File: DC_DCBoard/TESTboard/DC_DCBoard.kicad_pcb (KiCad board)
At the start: 2 copper layers, 137.2 x 68.6 mm, 26 parts, among them J1 TSV, J2 12V_OUT, J3 Conn_01x05, U1 DCM4623TD2J13D0T70, U2 LTV-817S, U3 TLP184, U4 LTV-817S

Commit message: Fixed pot value on test board
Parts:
- added R2: 6.8k, Resistor_SMD:R_0603_1608Metric, F.Cu at (106.0, 127.6)
- RV1: value 5k -> 50k; footprint Potentiometer_THT:Potentiometer_Piher_PT-15-V02_Vertical -> CustomFootprints:TC33X-503ECT-ND
- moved RV1 8.52 mm to (95.9, 125.1), turned to 270 degrees
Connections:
- RV1 pad 2: /HV- -> Net-(R2-Pad1)
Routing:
- net Net-(R2-Pad1): track 0.00 -> 6.79 mm
- net /TRIM: track 51.9 -> 58.5 mm, vias 0 -> 1
- net /HV-: track 164.4 -> 165.7 mm

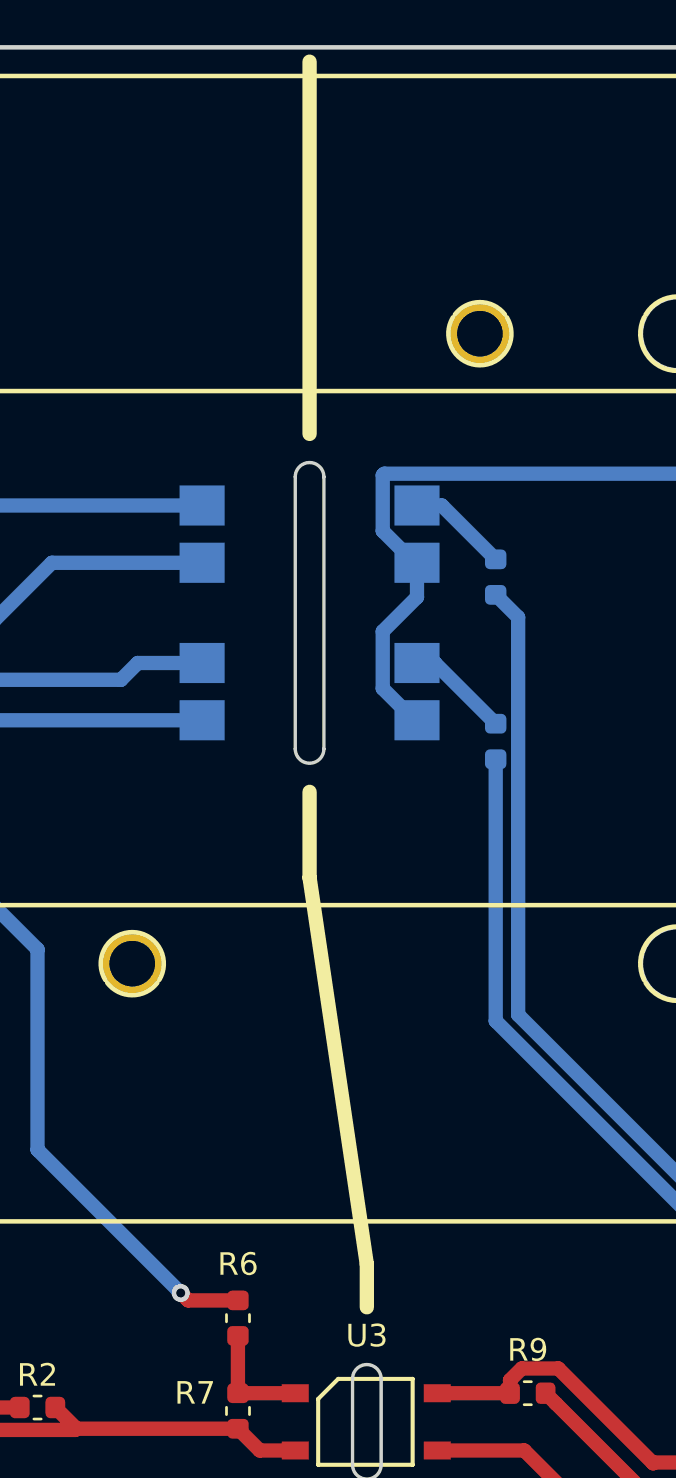
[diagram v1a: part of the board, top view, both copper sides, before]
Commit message: updated footprints
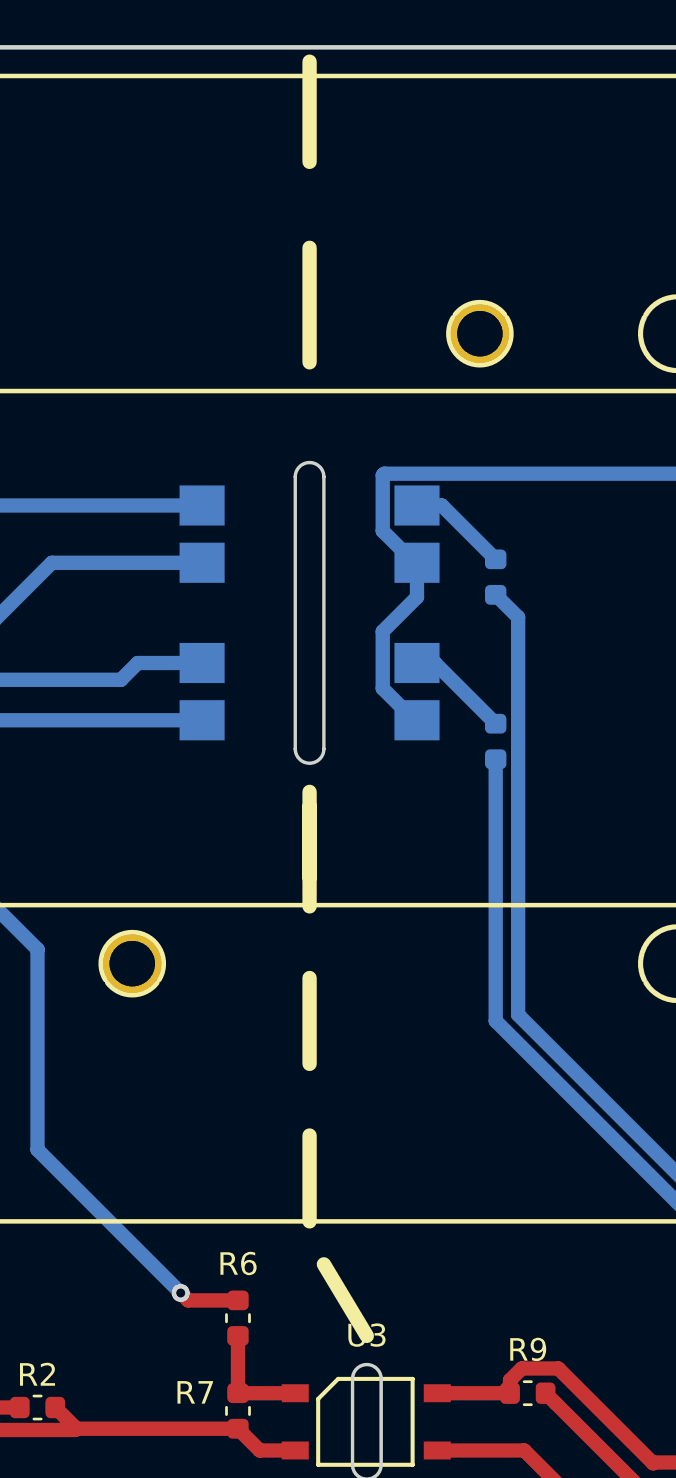
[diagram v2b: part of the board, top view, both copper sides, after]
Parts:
- added G***: LOGO, CustomFootprints:hvlightningsymbol, B.Cu at (74.3, 99.7)

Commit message: Getting there with layout of big board...
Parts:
- removed R7: 100k, Resistor_SMD:R_0603_1608Metric
- added REF**: MountingHole_4.3mm_M4, MountingHole:MountingHole_4.3mm_M4, F.Cu at (61.6, 71.8)
- added REF**: MountingHole_4.3mm_M4, MountingHole:MountingHole_4.3mm_M4, F.Cu at (189.9, 71.8)
- added REF**: MountingHole_4.3mm_M4, MountingHole:MountingHole_4.3mm_M4, F.Cu at (61.6, 131.4)
- added REF**: MountingHole_4.3mm_M4, MountingHole:MountingHole_4.3mm_M4, F.Cu at (189.9, 131.4)
- F1: footprint Fuse:Fuseholder_Cylinder-5x20mm_Schurter_0031_8201_Horizontal_Open -> CustomFootprints:Fuseholder_Cylinder-5x20mm_Schurter_0031_8201_Horizontal_Open_3d
- U1: footprint CustomFootprints:DCM4623TD2J13D0T70 w_landpattern -> CustomFootprints:DCM4623TD2J13D0T70_w_landpattern
- moved C2 2.54 mm to (69.8, 71.1)
- moved C3 1.91 mm to (78.7, 71.1)
- moved C1 1.27 mm to (87.6, 71.1)
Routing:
- net Net-(R6-Pad1): track 5.08 -> 3.59 mm
- net Net-(C1-Pad1): track 69.6 -> 68.9 mm
- net /HV-: track 165.7 -> 165.2 mm
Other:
- outline, holes or cut-outs redrawn
